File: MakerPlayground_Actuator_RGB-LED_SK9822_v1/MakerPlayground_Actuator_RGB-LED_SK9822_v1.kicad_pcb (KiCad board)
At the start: 2 copper layers, 30.4 x 19.9 mm, 6 parts, among them J1 Conn_01x04

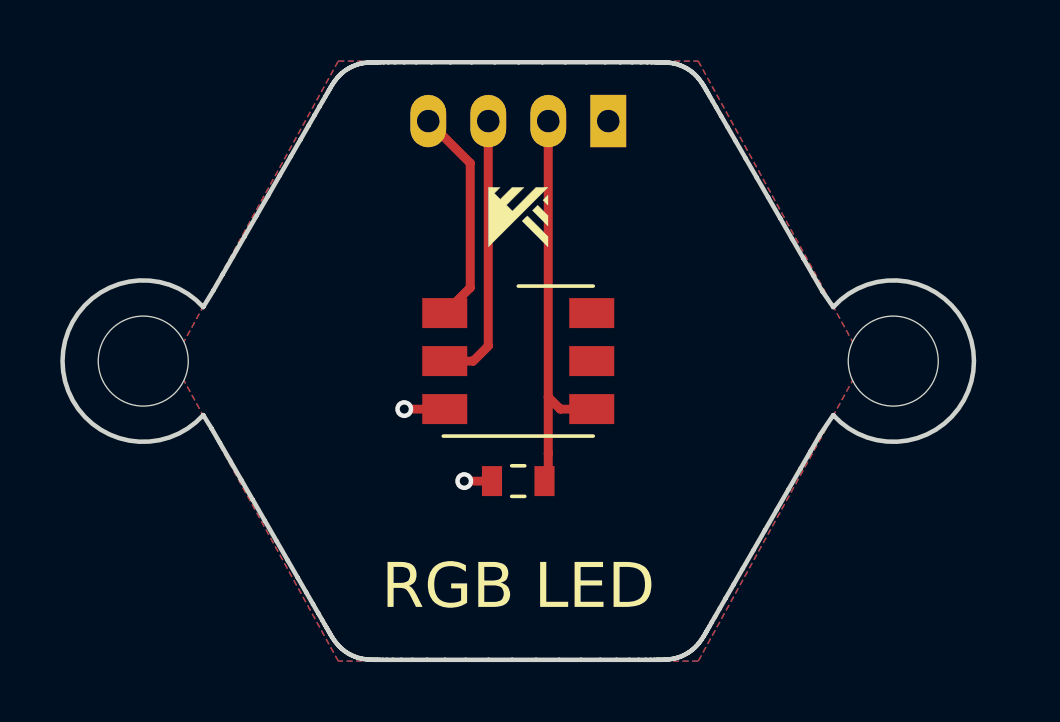
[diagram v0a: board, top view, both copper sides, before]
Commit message: RGB LED mounting hole barrier size experiment.
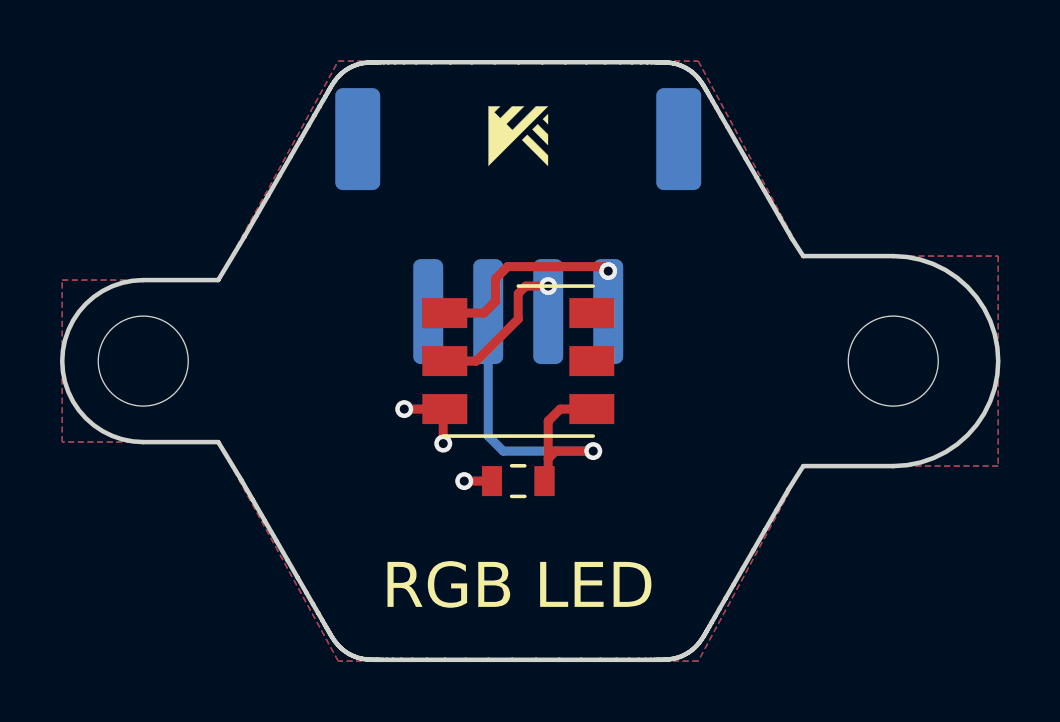
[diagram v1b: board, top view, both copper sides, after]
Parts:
- J1: footprint Connector_JST:JST_PH_S4B-PH-K_1x04_P2.00mm_Horizontal -> Connector_JST:JST_PH_S4B-PH-SM4-TB_1x04-1MP_P2.00mm_Horizontal
- moved J1 4.61 mm to (136.5, 95.5), turned to 0 degrees
- moved G*** 2.70 mm to (136.5, 92.5)
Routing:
- net Net-(J1-Pad3): track 9.16 -> 4.98 mm, vias 0 -> 1
- net GND: track 2.28 -> 3.45 mm, vias 2 -> 3
- net Net-(J1-Pad4): track 7.33 -> 6.59 mm, vias 0 -> 1
- net VCC: track 13.7 -> 13.1 mm, vias 0 -> 1
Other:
- board size 30.4 x 19.9 mm -> 31.2 x 19.9 mm
